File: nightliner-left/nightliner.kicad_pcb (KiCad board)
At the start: 2 copper layers, 154.8 x 116.1 mm, 83 parts, among them J1 TYPE-C-31-M-12, J2 Battery, J3 Serial, P1 ISP_Prog, SW1 pinky_top, SW10 inner_home, SW11 pinky_bottom, SW12 ring_bottom, SW13 middle_bottom, SW14 index_bottom, SW15 inner_bottom, SW16 outer_top, SW17 outer_home, SW18 near_thumb, SW19 home_thumb, SW2 ring_top, SW20 far_thumb, SW21 ON_OFF, SW22 RESET, SW3 middle_top, SW4 index_top, SW5 inner_top, SW6 pinky_home, SW7 ring_home, SW8 middle_home, SW9 index_home, U1 holyiot-18010, U2 TVS2200DRV, U3 USBLC6-2SC6, U4 BQ24075RGT, U5 XC6220B331MR

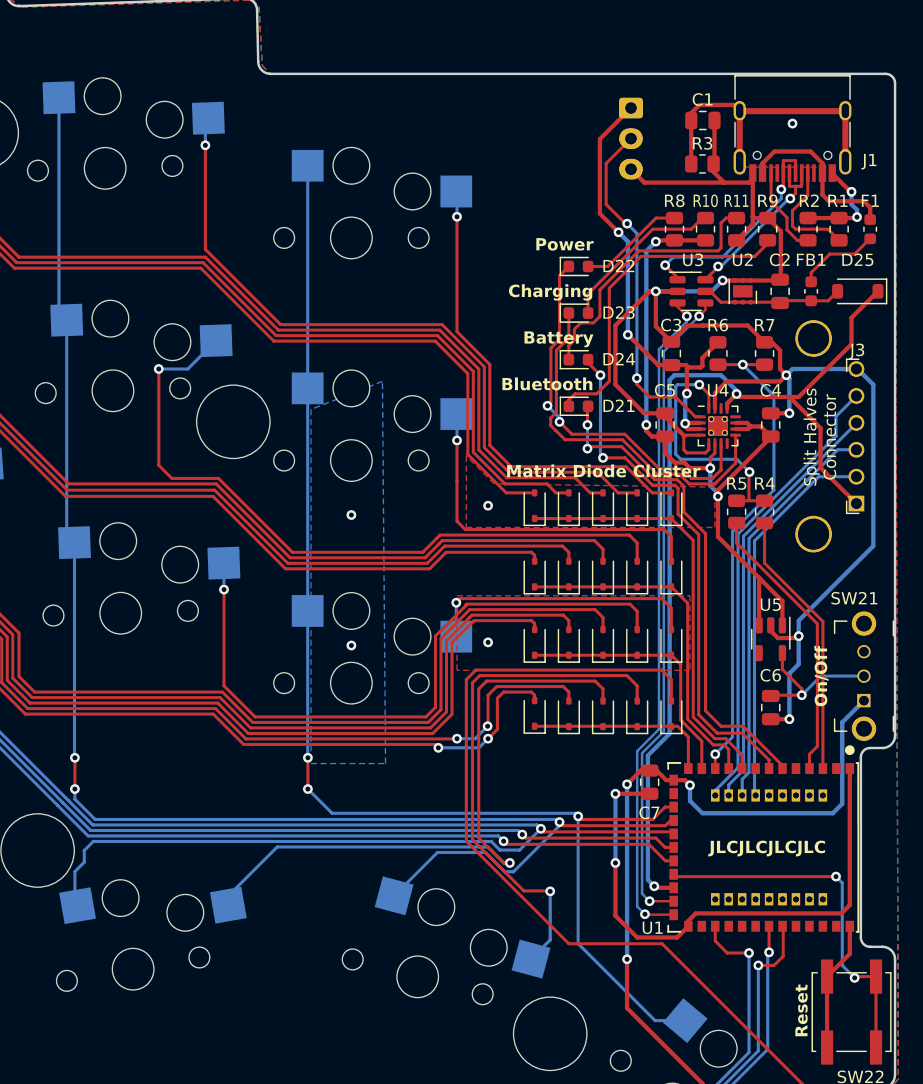
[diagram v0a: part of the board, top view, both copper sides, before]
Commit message: fix: make sides symmetric
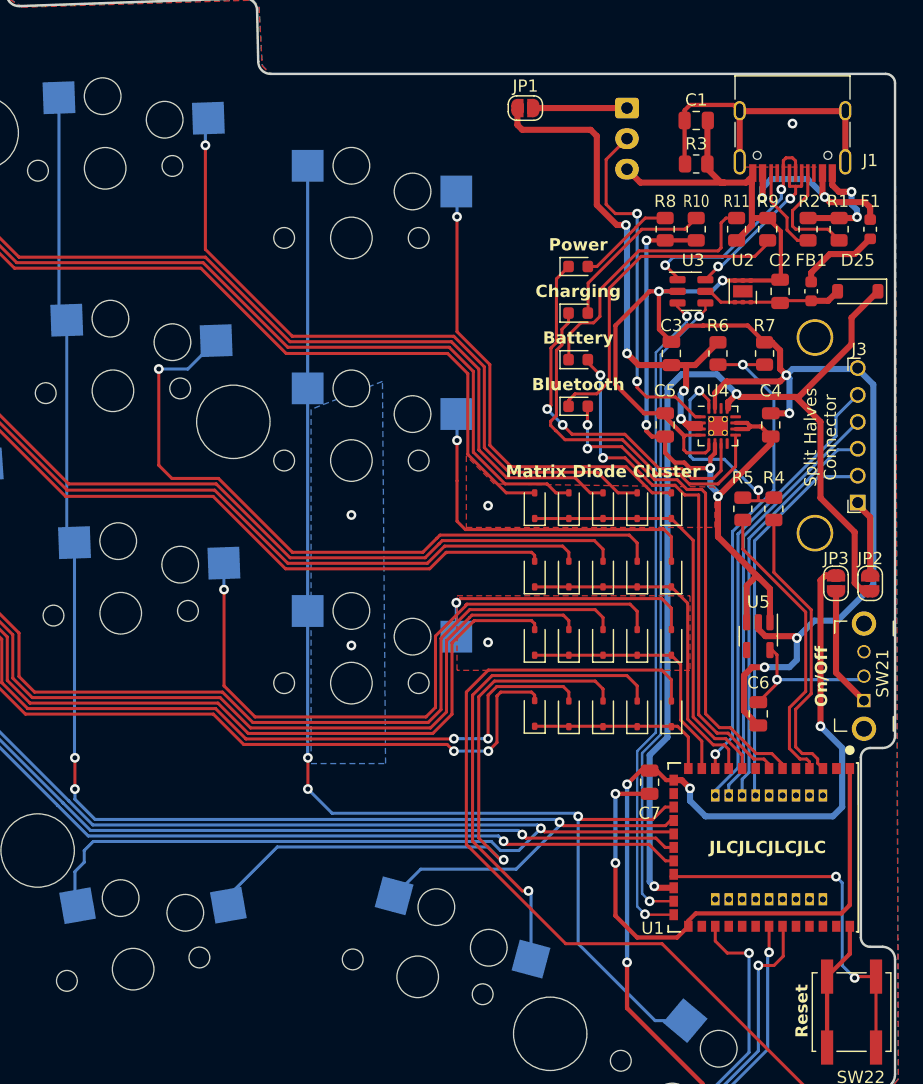
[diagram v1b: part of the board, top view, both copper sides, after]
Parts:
- added JP1: VBAT, Jumper:SolderJumper-2_P1.3mm_Open_RoundedPad1.0x1.5mm, F.Cu at (143.3, 40.4)
- added JP2: VBUS, Jumper:SolderJumper-2_P1.3mm_Open_RoundedPad1.0x1.5mm, F.Cu at (171.4, 79.2)
- added JP3: VDD, Jumper:SolderJumper-2_P1.3mm_Open_RoundedPad1.0x1.5mm, F.Cu at (168.7, 79.2)
- moved C6 1.14 mm to (162.3, 89.9)
- moved U5 1.05 mm to (162.3, 83.6)
- moved R4 0.80 mm to (163.6, 73.2)
- moved R10 0.76 mm to (157.2, 50.3)
- moved R8 0.76 mm to (154.7, 50.3)
- moved R5 0.57 mm to (161.0, 73.2)
- moved C1 0.55 mm to (157.2, 41.4)
- moved R3 0.51 mm to (157.2, 45.0)
- moved J2 0.33 mm to (151.6, 40.4)
- moved J3 0.14 mm to (170.4, 72.6)
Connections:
- J2 pad 1: /VBAT -> Net-(JP1-B)
- J3 pad 1: VBUS -> Net-(J3-Pin_1)
- SW21 pad 1: VDD -> Net-(JP3-A)
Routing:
- net VDD: track 71.2 -> 82.7 mm, vias 4 -> 5
- net Net-(JP3-A): track 0.00 -> 9.88 mm
- net VBUS: track 79.4 -> 87.2 mm
- net Net-(JP1-B): track 0.00 -> 7.66 mm
- net Net-(J3-Pin_1): track 0.00 -> 6.34 mm
- net /VBAT: track 38.0 -> 44.3 mm
- net GND: track 199.9 -> 204.7 mm
- net Net-(U4-ISET): track 21.1 -> 17.5 mm
- net Net-(D19-A): track 42.4 -> 39.6 mm
- net Net-(F1-Pad1): track 14.4 -> 16.0 mm, vias 0 -> 2
- net Net-(D18-A): track 53.2 -> 51.6 mm
- net CHARGE_CTRL_1: track 22.0 -> 23.5 mm
- net COL3: track 125.7 -> 124.4 mm
- net /BAT_TEMP: track 28.3 -> 29.3 mm
- net Net-(D16-A): track 147.3 -> 148.3 mm
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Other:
- board text added: "v1.0"

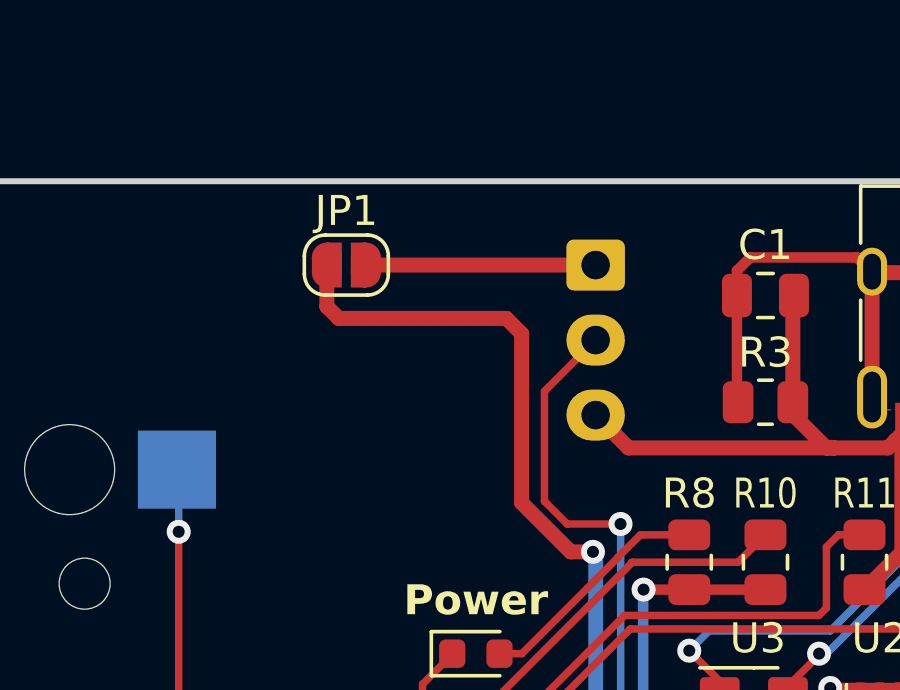
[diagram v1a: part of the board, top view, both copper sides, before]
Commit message: feat: initial right side case completed
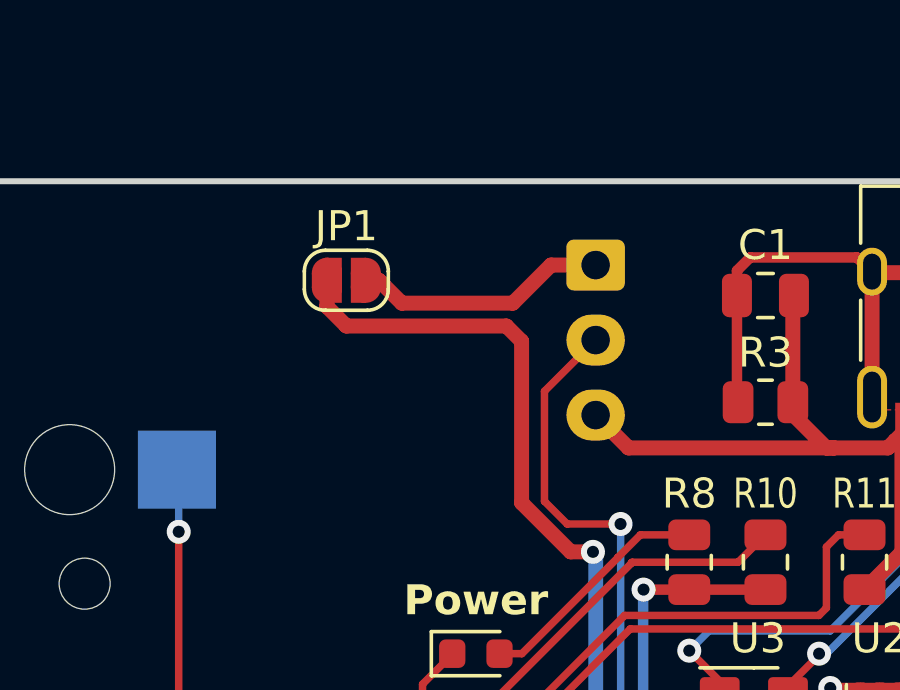
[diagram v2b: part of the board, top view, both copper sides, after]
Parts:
- P1: value ISP_Prog -> ISP
- moved JP1 0.51 mm to (143.3, 40.9)
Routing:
- net Net-(JP1-B): track 7.66 -> 8.50 mm

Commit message: fix: change edge outline, flip switches
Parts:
- added JP4: VBUS, Jumper:SolderJumper-2_P1.3mm_Open_RoundedPad1.0x1.5mm, F.Cu at (150.9, 103.4)
- P1: value ISP -> ISP_Prog
- SW21: moved to B.Cu
- moved P1 18.6 mm to (141.4, 124.5), turned to 165 degrees
- moved JP1 4.10 mm to (147.3, 40.4)
- moved SW21 3.97 mm to (170.9, 84.9), turned to -90 degrees
- moved H6 1.48 mm to (102.1, 100.3)
- moved H7 0.80 mm to (145.5, 115.3)
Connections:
- SW21 pad 1: Net-(JP3-A) -> unconnected-(SW21-A-Pad1)
- SW21 pad 3: unconnected-(SW21-C-Pad3) -> Net-(JP3-A)
- U1 pad 47: VBUS -> Net-(JP4-B)
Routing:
- net GND: track 204.7 -> 252.0 mm, vias 15 -> 17
- net SWO: track 33.7 -> 50.7 mm
- net SWDIO: track 31.4 -> 48.1 mm
- net SWCLK: track 29.8 -> 45.9 mm
- net Net-(JP1-B): track 8.50 -> 3.60 mm
- net Net-(JP4-B): track 0.00 -> 4.55 mm
- net /VBAT: track 44.2 -> 40.3 mm
- net VDD: track 82.7 -> 83.8 mm
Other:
- outline, holes or cut-outs redrawn
